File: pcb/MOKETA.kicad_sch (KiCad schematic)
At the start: 130 parts, among them SW43 Reset, U1 Pro_Micro

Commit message: Basic routing
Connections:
- net VCC: now also LED39.1 (VDD), LED40.1 (VDD)
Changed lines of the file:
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@@
+	)
+	(junction
+		(at 123.19 184.15)
+		(diameter 0)
+		(color 0 0 0 0)
 	)
 	(junction
@@
 	(wire
 		(pts
+			(xy 123.19 184.15) (xy 128.27 184.15)
+		)
+		(stroke
+			(width 0)
+			(type default)
+		)
+	)
+	(wire
+		(pts
 			(xy 74.93 40.64) (xy 74.93 25.4)
 		)
@@
 	(wire
 		(pts
+			(xy 123.19 105.41) (xy 123.19 184.15)
+		)
+		(stroke
+			(width 0)
+			(type default)
+		)
+	)
+	(wire
+		(pts
 			(xy 127 170.18) (xy 127 133.35)
 		)
@@
 	(wire
 		(pts
-			(xy 116.84 184.15) (xy 128.27 184.15)
-		)
-		(stroke
+			(xy 116.84 184.15) (xy 123.19 184.15)
+		)
+		(stroke

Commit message: change footrpint
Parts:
- SW44: footprint moketa:BSI-10H -> moketa:MSK-12C02
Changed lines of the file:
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@@
 			)
 		)
-		(property "Footprint" "moketa:BSI-10H"
+		(property "Footprint" "moketa:MSK-12C02"
 			(at 123.444 249.174 0)
 			(effects

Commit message: add footrpint
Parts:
- added D43, D44, D45, D46: ~, moketa:LED_1206, symbol moketa:LED
- added J2, J3: ~, moketa:FFC_CMD_1x20_P0.5mm, symbol moketa:CONN_01x20
- added R1, R2, R3, R4: ~, moketa:R_1206_3216, symbol moketa:RESISTOR
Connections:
- net GND: now also D43.1 (K), D44.1 (K), D45.1 (K), D46.1 (K)
- net LED2: now reaches U1.11 (8/B4)
- net LED2: now also R2.1
- net LED3: now reaches U1.12 (9/B5)
- net LED3: now also R3.1
- net LED4: now reaches U1.14 (B2/16)
- net LED4: now also R4.1
- net LED1: now reaches U1.2 (RX1/D2)
- net LED1: now also R1.1
- net LED renamed LEDS
- new net: D46.2 (A), R4.2
- new net: D44.2 (A), R2.2
- new net: D43.2 (A), R1.2
- new net: D45.2 (A), R3.2

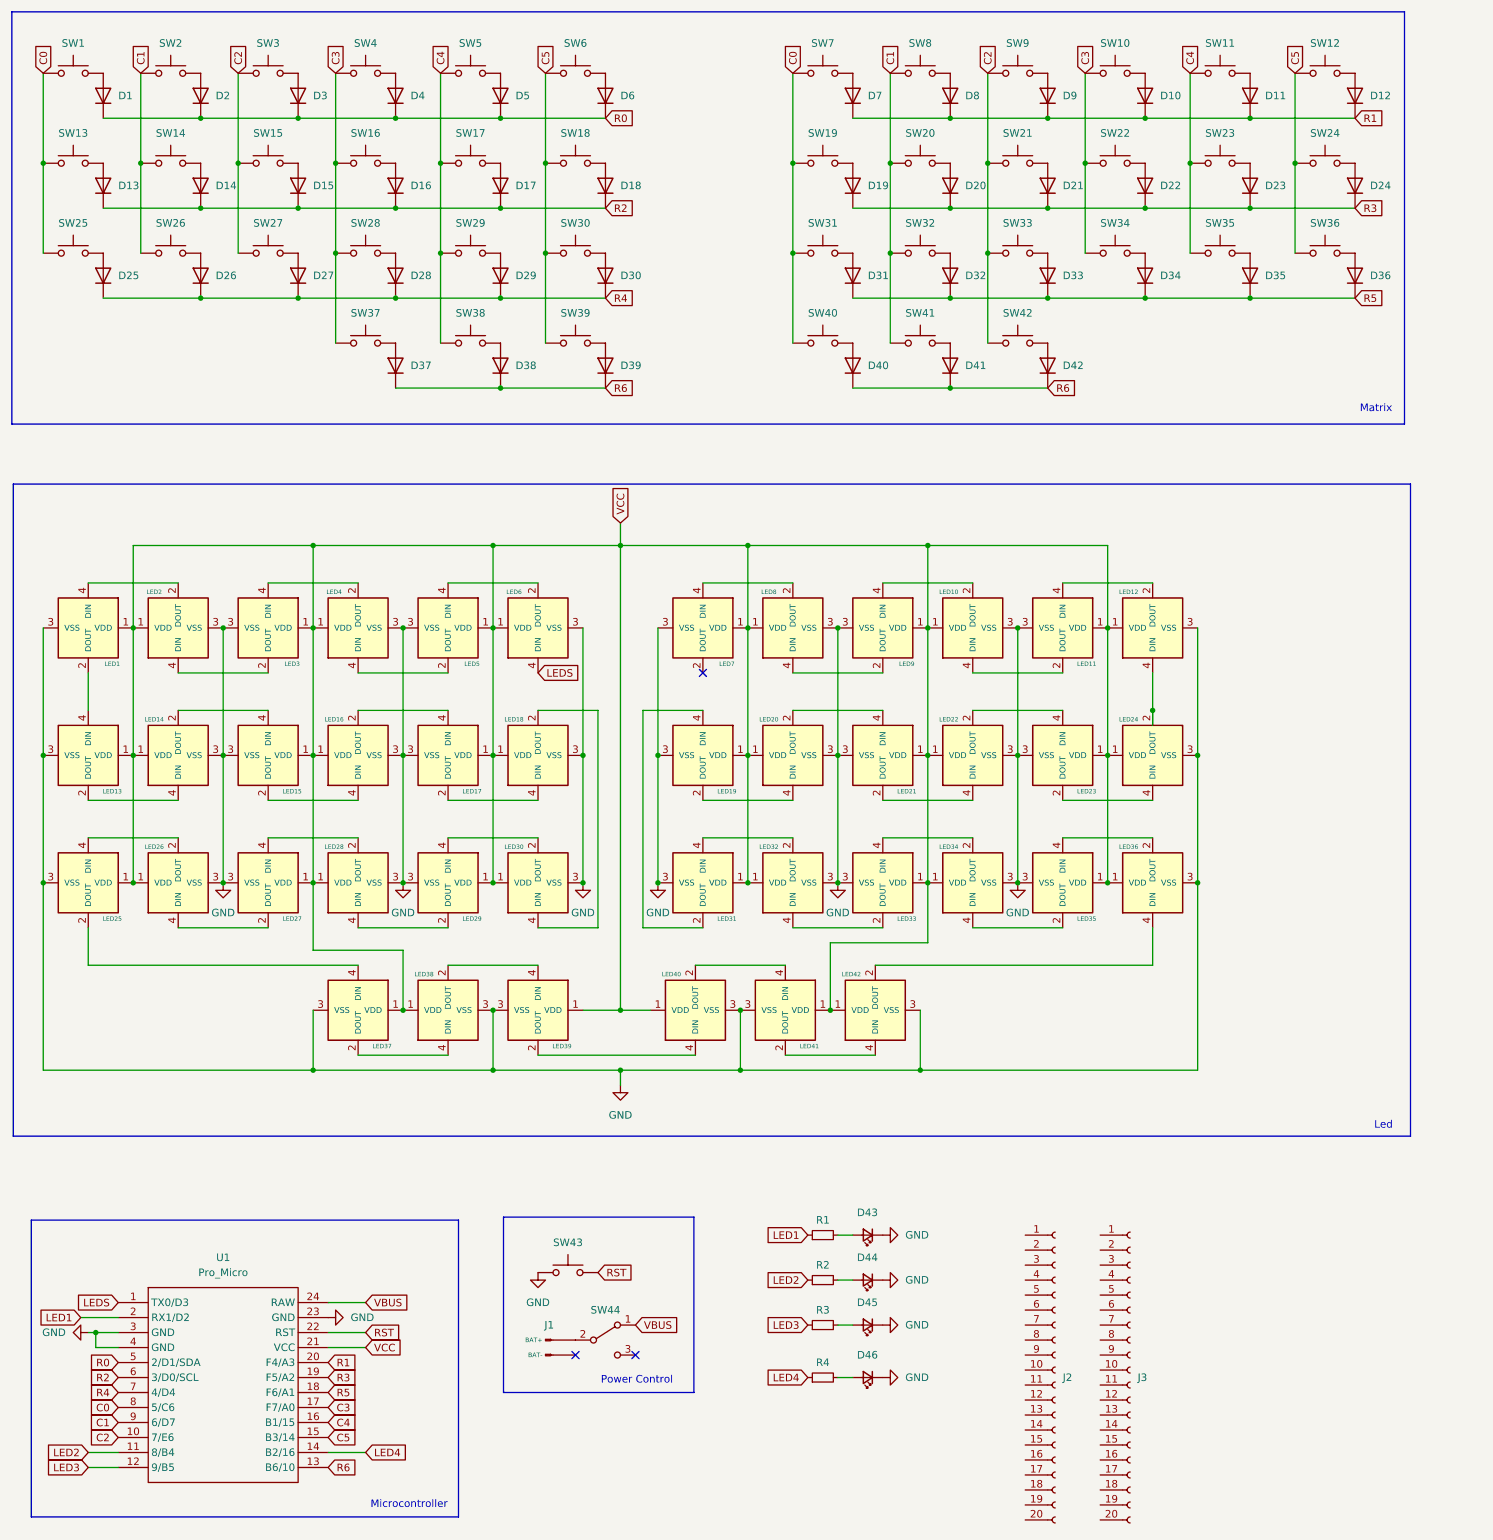
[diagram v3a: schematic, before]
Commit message: Basic routing on almost whole board
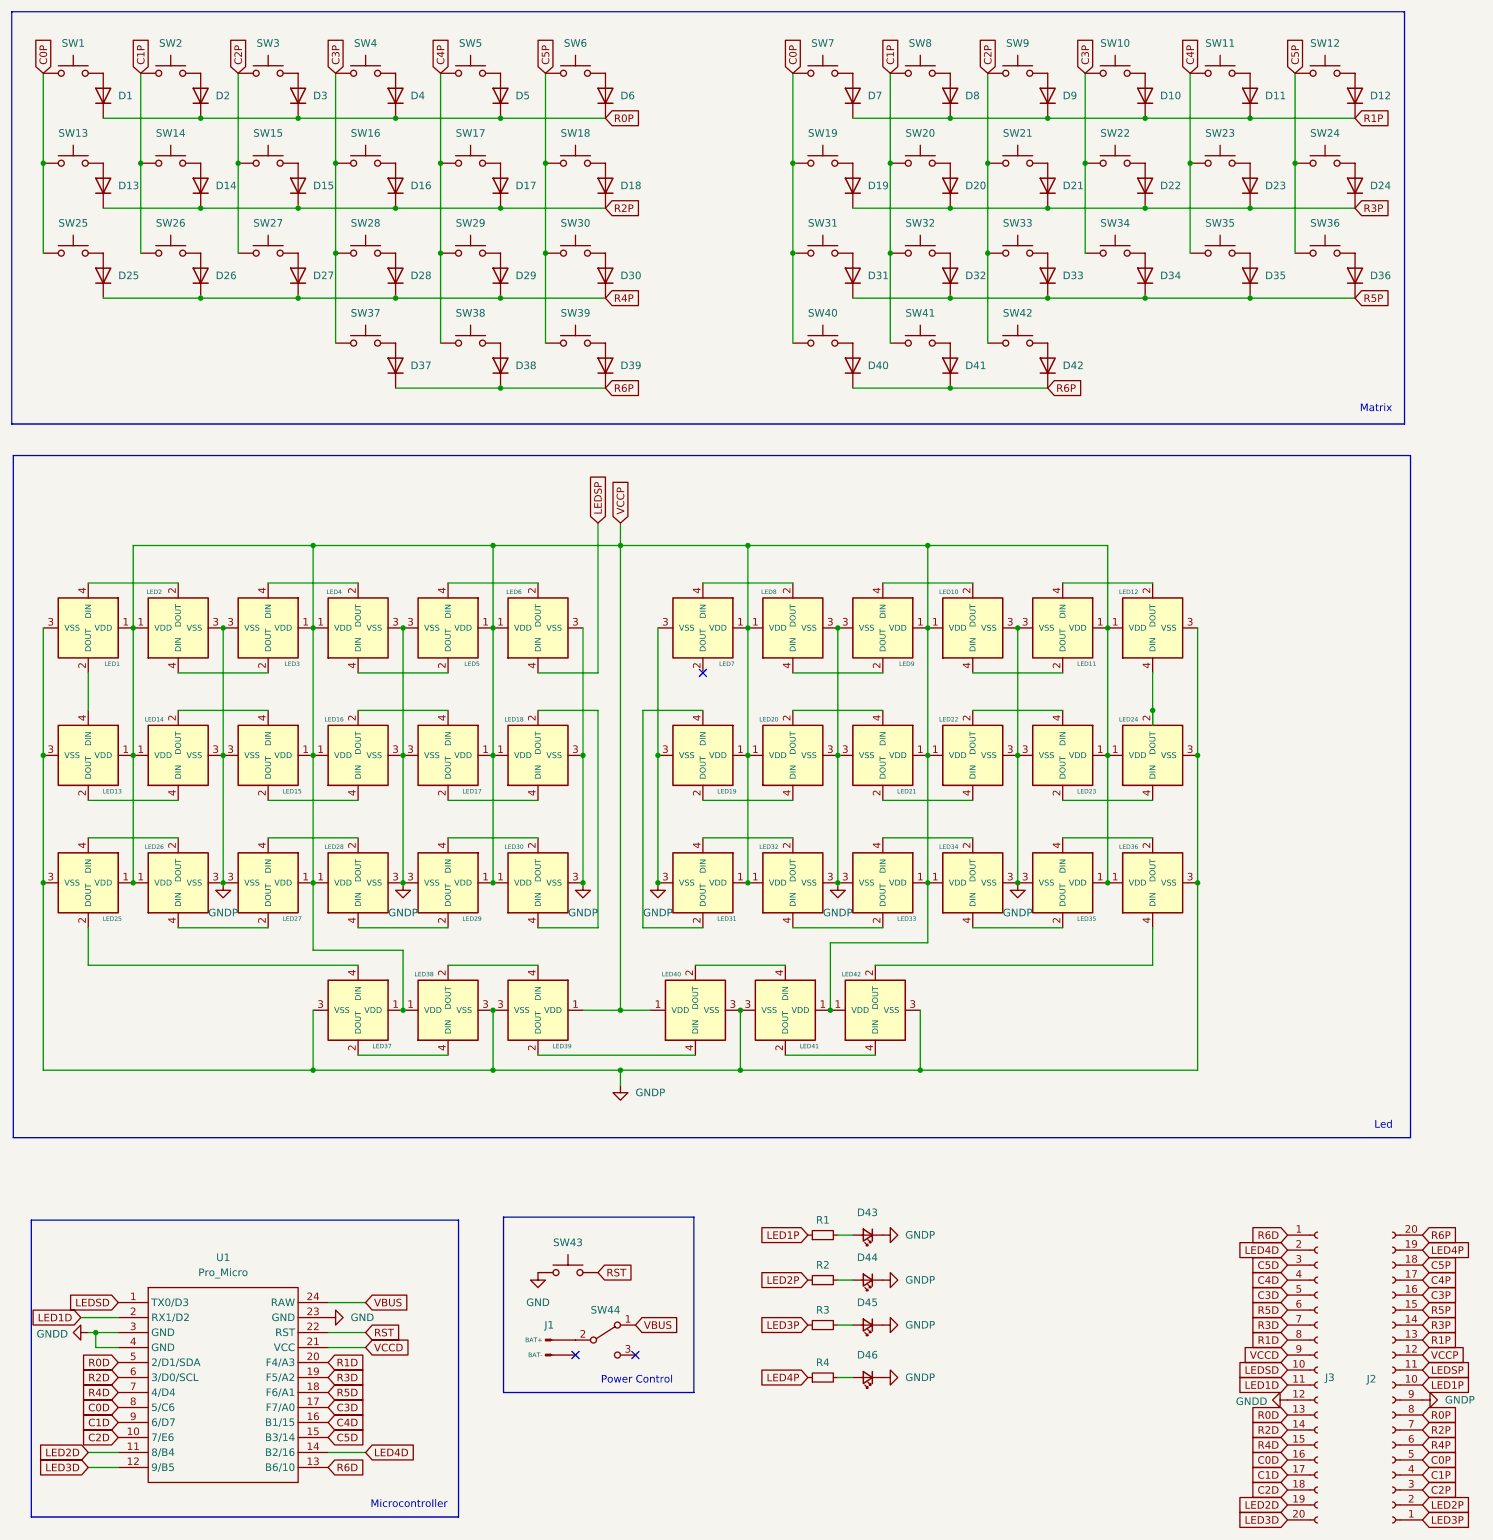
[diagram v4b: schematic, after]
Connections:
- net GND: no longer D43.1 (K), D44.1 (K), D45.1 (K), D46.1 (K), LED1.3 (VSS), LED10.3 (VSS), LED11.3 (VSS), LED12.3 (VSS), LED13.3 (VSS), LED14.3 (VSS), LED15.3 (VSS), LED16.3 (VSS), LED17.3 (VSS), LED18.3 (VSS), LED19.3 (VSS), LED2.3 (VSS), LED20.3 (VSS), LED21.3 (VSS), LED22.3 (VSS), LED23.3 (VSS), LED24.3 (VSS), LED25.3 (VSS), LED26.3 (VSS), LED27.3 (VSS), LED28.3 (VSS), LED29.3 (VSS), LED3.3 (VSS), LED30.3 (VSS), LED31.3 (VSS), LED32.3 (VSS), LED33.3 (VSS), LED34.3 (VSS), LED35.3 (VSS), LED36.3 (VSS), LED37.3 (VSS), LED38.3 (VSS), LED39.3 (VSS), LED4.3 (VSS), LED40.3 (VSS), LED41.3 (VSS), LED42.3 (VSS), LED5.3 (VSS), LED6.3 (VSS), LED7.3 (VSS), LED8.3 (VSS), LED9.3 (VSS), U1.3 (GND), U1.4 (GND)
- net R6D: now reaches J3.1 (Pin_1)
- net R6D: now also U1.13 (B6/10)
- net LEDSD: now reaches J3.10 (Pin_10)
- net LEDSD: now also U1.1 (TX0/D3)
- net LED1D: now reaches J3.11 (Pin_11)
- net LED1D: now also U1.2 (RX1/D2)
- net GNDD: now reaches J3.12 (Pin_12)
- net GNDD: now also U1.3 (GND), U1.4 (GND)
- net R0D: now reaches J3.13 (Pin_13)
- net R0D: now also U1.5 (2/D1/SDA)
- net R2D: now reaches J3.14 (Pin_14)
- net R2D: now also U1.6 (3/D0/SCL)
- net R4D: now reaches J3.15 (Pin_15)
- net R4D: now also U1.7 (4/D4)
- net C0D: now reaches J3.16 (Pin_16)
- net C0D: now also U1.8 (5/C6)
- net C1D: now reaches J3.17 (Pin_17)
- net C1D: now also U1.9 (6/D7)
- net C2D: now reaches J3.18 (Pin_18)
- net C2D: now also U1.10 (7/E6)
- net LED2D: now reaches J3.19 (Pin_19)
- net LED2D: now also U1.11 (8/B4)
- net LED4D: now reaches J3.2 (Pin_2)
- net LED4D: now also U1.14 (B2/16)
- net LED3D: now reaches J3.20 (Pin_20)
- net LED3D: now also U1.12 (9/B5)
- net C5D: now reaches J3.3 (Pin_3)
- net C5D: now also U1.15 (B3/14)
- net C4D: now reaches J3.4 (Pin_4)
- net C4D: now also U1.16 (B1/15)
- net C3D: now reaches J3.5 (Pin_5)
- net C3D: now also U1.17 (F7/A0)
- net R5D: now reaches J3.6 (Pin_6)
- net R5D: now also U1.18 (F6/A1)
- net R3D: now reaches J3.7 (Pin_7)
- net R3D: now also U1.19 (F5/A2)
- net R1D: now reaches J3.8 (Pin_8)
- net R1D: now also U1.20 (F4/A3)
- net VCCD: now reaches J3.9 (Pin_9)
- net VCCD: now also U1.21 (VCC)
- net LED3P: now reaches J2.1 (Pin_1)
- net LED3P: now also R3.1
- net LED1P: now reaches J2.10 (Pin_10)
- net LED1P: now also R1.1
- net LEDSP: now reaches J2.11 (Pin_11)
- net LEDSP: now also LED6.4 (DIN)
- net VCCP: now reaches J2.12 (Pin_12)
- net VCCP: now also LED1.1 (VDD), LED10.1 (VDD), LED11.1 (VDD), LED12.1 (VDD), LED13.1 (VDD), LED14.1 (VDD), LED15.1 (VDD), LED16.1 (VDD), LED17.1 (VDD), LED18.1 (VDD), LED19.1 (VDD), LED2.1 (VDD), LED20.1 (VDD), LED21.1 (VDD), LED22.1 (VDD), LED23.1 (VDD), LED24.1 (VDD), LED25.1 (VDD), LED26.1 (VDD), LED27.1 (VDD), LED28.1 (VDD), LED29.1 (VDD), LED3.1 (VDD), LED30.1 (VDD), LED31.1 (VDD), LED32.1 (VDD), LED33.1 (VDD), LED34.1 (VDD), LED35.1 (VDD), LED36.1 (VDD), LED37.1 (VDD), LED38.1 (VDD), LED39.1 (VDD), LED4.1 (VDD), LED40.1 (VDD), LED41.1 (VDD), LED42.1 (VDD), LED5.1 (VDD), LED6.1 (VDD), LED7.1 (VDD), LED8.1 (VDD), LED9.1 (VDD)
- net R1P: now reaches J2.13 (Pin_13)
- net R1P: now also D10.1 (K), D11.1 (K), D12.1 (K), D7.1 (K), D8.1 (K), D9.1 (K)
- net R3P: now reaches J2.14 (Pin_14)
- net R3P: now also D19.1 (K), D20.1 (K), D21.1 (K), D22.1 (K), D23.1 (K), D24.1 (K)
- net R5P: now reaches J2.15 (Pin_15)
- net R5P: now also D31.1 (K), D32.1 (K), D33.1 (K), D34.1 (K), D35.1 (K), D36.1 (K)
- net C3P: now reaches J2.16 (Pin_16)
- net C3P: now also SW10.1, SW16.1, SW22.1, SW28.1, SW34.1, SW37.1, SW4.1
- net C4P: now reaches J2.17 (Pin_17)
- net C4P: now also SW11.1, SW17.1, SW23.1, SW29.1, SW35.1, SW38.1, SW5.1
- net C5P: now reaches J2.18 (Pin_18)
- net C5P: now also SW12.1, SW18.1, SW24.1, SW30.1, SW36.1, SW39.1, SW6.1
- net LED4P: now reaches J2.19 (Pin_19)
- net LED4P: now also R4.1
- net LED2P: now reaches J2.2 (Pin_2)
- net LED2P: now also R2.1
- net R6P: now reaches J2.20 (Pin_20)
- net R6P: now also D37.1 (K), D38.1 (K), D39.1 (K), D40.1 (K), D41.1 (K), D42.1 (K)
- net C2P: now reaches J2.3 (Pin_3)
- net C2P: now also SW15.1, SW21.1, SW27.1, SW3.1, SW33.1, SW42.1, SW9.1
- net C1P: now reaches J2.4 (Pin_4)
- net C1P: now also SW14.1, SW2.1, SW20.1, SW26.1, SW32.1, SW41.1, SW8.1
- net C0P: now reaches J2.5 (Pin_5)
- net C0P: now also SW1.1, SW13.1, SW19.1, SW25.1, SW31.1, SW40.1, SW7.1
- net R4P: now reaches J2.6 (Pin_6)
- net R4P: now also D25.1 (K), D26.1 (K), D27.1 (K), D28.1 (K), D29.1 (K), D30.1 (K)
- net R2P: now reaches J2.7 (Pin_7)
- net R2P: now also D13.1 (K), D14.1 (K), D15.1 (K), D16.1 (K), D17.1 (K), D18.1 (K)
- net R0P: now reaches J2.8 (Pin_8)
- net R0P: now also D1.1 (K), D2.1 (K), D3.1 (K), D4.1 (K), D5.1 (K), D6.1 (K)
- net GNDP: now reaches J2.9 (Pin_9)
- net GNDP: now also D43.1 (K), D44.1 (K), D45.1 (K), D46.1 (K), LED1.3 (VSS), LED10.3 (VSS), LED11.3 (VSS), LED12.3 (VSS), LED13.3 (VSS), LED14.3 (VSS), LED15.3 (VSS), LED16.3 (VSS), LED17.3 (VSS), LED18.3 (VSS), LED19.3 (VSS), LED2.3 (VSS), LED20.3 (VSS), LED21.3 (VSS), LED22.3 (VSS), LED23.3 (VSS), LED24.3 (VSS), LED25.3 (VSS), LED26.3 (VSS), LED27.3 (VSS), LED28.3 (VSS), LED29.3 (VSS), LED3.3 (VSS), LED30.3 (VSS), LED31.3 (VSS), LED32.3 (VSS), LED33.3 (VSS), LED34.3 (VSS), LED35.3 (VSS), LED36.3 (VSS), LED37.3 (VSS), LED38.3 (VSS), LED39.3 (VSS), LED4.3 (VSS), LED40.3 (VSS), LED41.3 (VSS), LED42.3 (VSS), LED5.3 (VSS), LED6.3 (VSS), LED7.3 (VSS), LED8.3 (VSS), LED9.3 (VSS)
- removed net C0: SW1.1, SW13.1, SW19.1, SW25.1, SW31.1, SW40.1, SW7.1, U1.8 (5/C6)
- removed net C1: SW14.1, SW2.1, SW20.1, SW26.1, SW32.1, SW41.1, SW8.1, U1.9 (6/D7)
- removed net C2: SW15.1, SW21.1, SW27.1, SW3.1, SW33.1, SW42.1, SW9.1, U1.10 (7/E6)
- removed net C3: SW10.1, SW16.1, SW22.1, SW28.1, SW34.1, SW37.1, SW4.1, U1.17 (F7/A0)
- removed net C4: SW11.1, SW17.1, SW23.1, SW29.1, SW35.1, SW38.1, SW5.1, U1.16 (B1/15)
- removed net C5: SW12.1, SW18.1, SW24.1, SW30.1, SW36.1, SW39.1, SW6.1, U1.15 (B3/14)
- removed net LED1: R1.1, U1.2 (RX1/D2)
- removed net LED2: R2.1, U1.11 (8/B4)
- removed net LED3: R3.1, U1.12 (9/B5)
- removed net LED4: R4.1, U1.14 (B2/16)
- removed net LEDS: LED6.4 (DIN), U1.1 (TX0/D3)
- removed net R0: D1.1 (K), D2.1 (K), D3.1 (K), D4.1 (K), D5.1 (K), D6.1 (K), U1.5 (2/D1/SDA)
- removed net R1: D10.1 (K), D11.1 (K), D12.1 (K), D7.1 (K), D8.1 (K), D9.1 (K), U1.20 (F4/A3)
- removed net R2: D13.1 (K), D14.1 (K), D15.1 (K), D16.1 (K), D17.1 (K), D18.1 (K), U1.6 (3/D0/SCL)
- removed net R3: D19.1 (K), D20.1 (K), D21.1 (K), D22.1 (K), D23.1 (K), D24.1 (K), U1.19 (F5/A2)
- removed net R4: D25.1 (K), D26.1 (K), D27.1 (K), D28.1 (K), D29.1 (K), D30.1 (K), U1.7 (4/D4)
- removed net R5: D31.1 (K), D32.1 (K), D33.1 (K), D34.1 (K), D35.1 (K), D36.1 (K), U1.18 (F6/A1)
- removed net R6: D37.1 (K), D38.1 (K), D39.1 (K), D40.1 (K), D41.1 (K), D42.1 (K), U1.13 (B6/10)
- removed net VCC: LED1.1 (VDD), LED10.1 (VDD), LED11.1 (VDD), LED12.1 (VDD), LED13.1 (VDD), LED14.1 (VDD), LED15.1 (VDD), LED16.1 (VDD), LED17.1 (VDD), LED18.1 (VDD), LED19.1 (VDD), LED2.1 (VDD), LED20.1 (VDD), LED21.1 (VDD), LED22.1 (VDD), LED23.1 (VDD), LED24.1 (VDD), LED25.1 (VDD), LED26.1 (VDD), LED27.1 (VDD), LED28.1 (VDD), LED29.1 (VDD), LED3.1 (VDD), LED30.1 (VDD), LED31.1 (VDD), LED32.1 (VDD), LED33.1 (VDD), LED34.1 (VDD), LED35.1 (VDD), LED36.1 (VDD), LED37.1 (VDD), LED38.1 (VDD), LED39.1 (VDD), LED4.1 (VDD), LED40.1 (VDD), LED41.1 (VDD), LED42.1 (VDD), LED5.1 (VDD), LED6.1 (VDD), LED7.1 (VDD), LED8.1 (VDD), LED9.1 (VDD), U1.21 (VCC)
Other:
- moved on the sheet: J2, J3

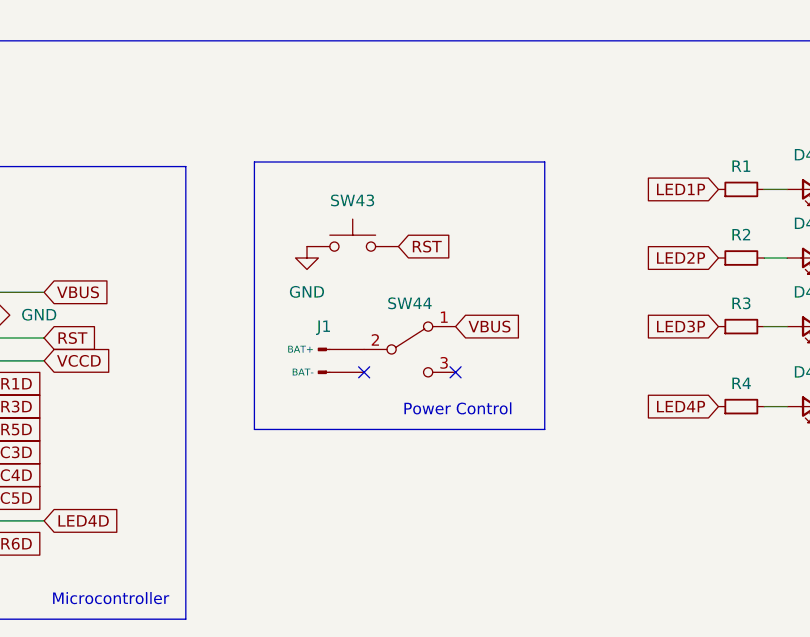
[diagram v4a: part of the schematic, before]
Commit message: Extended board, 38 mm between thumbs
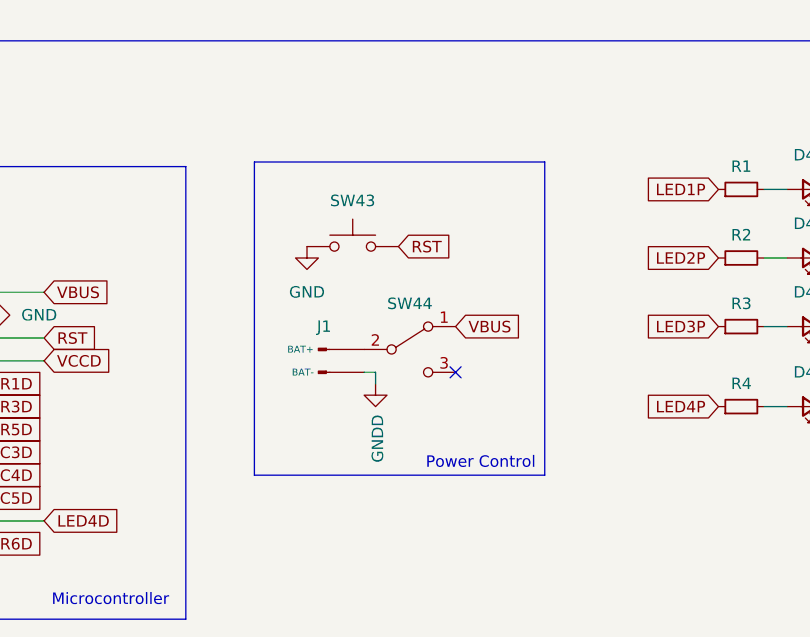
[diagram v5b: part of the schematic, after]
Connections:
- net GNDD: now also J1.2 (BAT-)
- no-connect marks 3 -> 2
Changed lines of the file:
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@@
 	(rectangle
 		(start 103.378 219.202)
-		(end 135.636 248.92)
+		(end 135.636 254)
 		(stroke
 			(width 0)
@@
 	(text "Power Control\n"
 		(exclude_from_sim no)
-		(at 125.984 246.888 0)
+		(at 128.524 252.73 0)
 		(effects
 			(font
@@
 	)
 	(no_connect
-		(at 115.57 242.57)
-	)
-	(no_connect
 		(at 125.73 242.57)
 	)
@@
 	(wire
 		(pts
+			(xy 115.57 242.57) (xy 116.84 242.57)
+		)
+		(stroke
+			(width 0)
+			(type default)
+		)
+	)
+	(wire
+		(pts
 			(xy 63.5 148.59) (xy 78.74 148.59)
 		)
@@
 	(wire
 		(pts
+			(xy 116.84 242.57) (xy 116.84 243.84)
+		)
+		(stroke
+			(width 0)
+			(type default)
+		)
+	)
+	(wire
+		(pts
 			(xy 168.91 25.4) (xy 168.91 40.64)
 		)
@@
 					(unit 1)
 				)
+			)
+		)
+	)
+	(symbol
+		(lib_id "moketa:GND")
+		(at 116.84 243.84 0)
+		(unit 1)
+		(exclude_from_sim no)
+		(in_bom yes)
+		(on_board yes)
+		(dnp no)
+		(property "Reference" "#PWR017"
+			(at 116.84 250.19 0)
+			(effects
+				(font
+					(size 1.27 1.27)
+				)
+				(hide yes)
+			)
+		)
+		(property "Value" "GNDD"
+			(at 117.094 249.936 90)
+			(effects
+				(font
+					(size 1.27 1.27)
+				)
+			)
+		)
+		(property "Footprint" ""
+			(at 116.84 243.84 0)
+			(effects
+				(font
+					(size 1.27 1.27)
+				)
+				(hide yes)
+			)
+		)
+		(property "Datasheet" ""
+			(at 116.84 243.84 0)
+			(effects
+				(font
+					(size 1.27 1.27)
+				)
+				(hide yes)
+			)
+		)
+		(property "Description" ""
+			(at 116.84 243.84 0)
+			(effects
+				(font
+					(size 1.27 1.27)
+				)
+				(hide yes)
+			)
+		)
+		(pin "1"
+		)
+		(instances
+			(project "MOKETA"
+				(path "/9e45a776-7007-48ff-b543-dc98423173b7"
+					(reference "#PWR017")
+					(unit 1)
+				)
